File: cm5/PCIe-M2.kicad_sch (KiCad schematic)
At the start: 39 parts, among them J1 67910-5700, J4 0786463001, M1 M.2 Screw, M2 M.2 Solder Nut, M3 M.2 Solder Nut, M4 M.2 Solder Nut, M5 M.2 Solder Nut, U1 CAT24C128, U8 AP3441SHE-7B

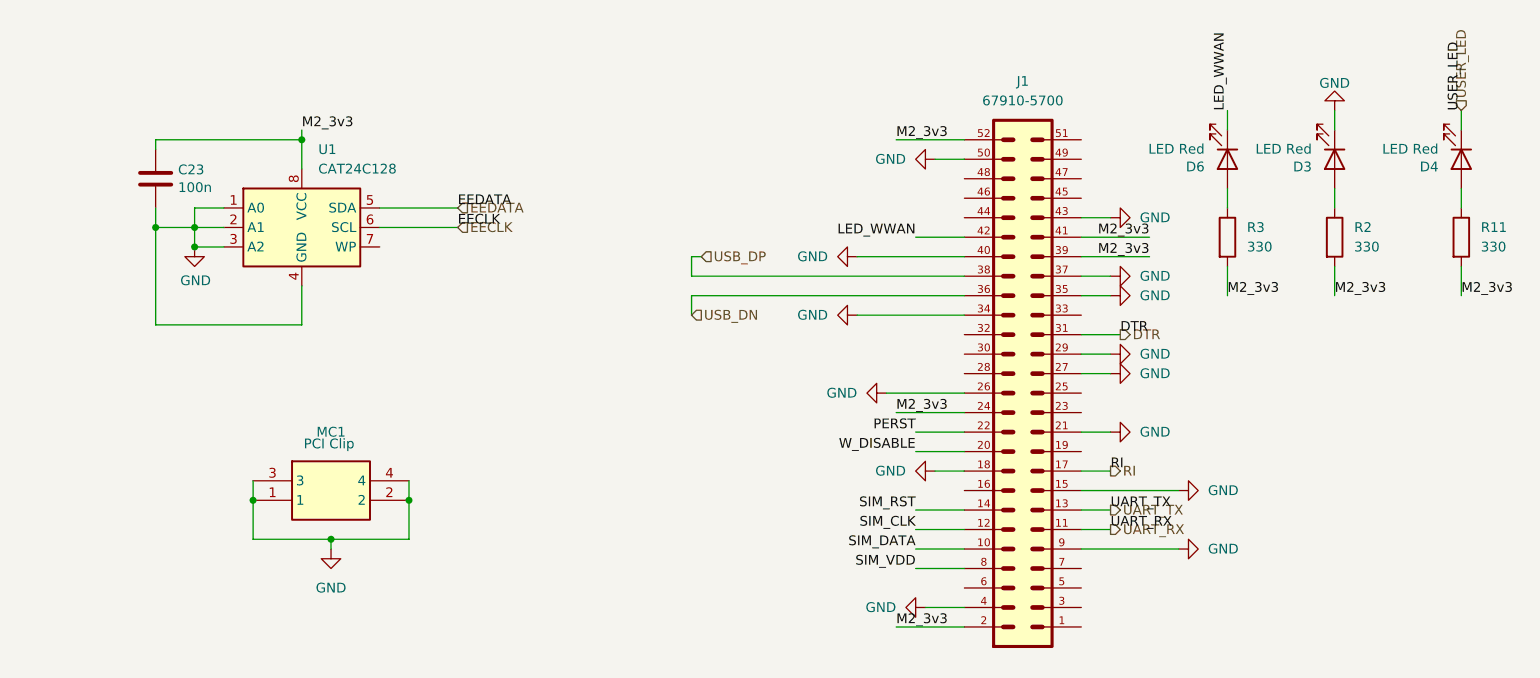
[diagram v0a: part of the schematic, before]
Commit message: Uh in this version, I have made the 5v trace fatter
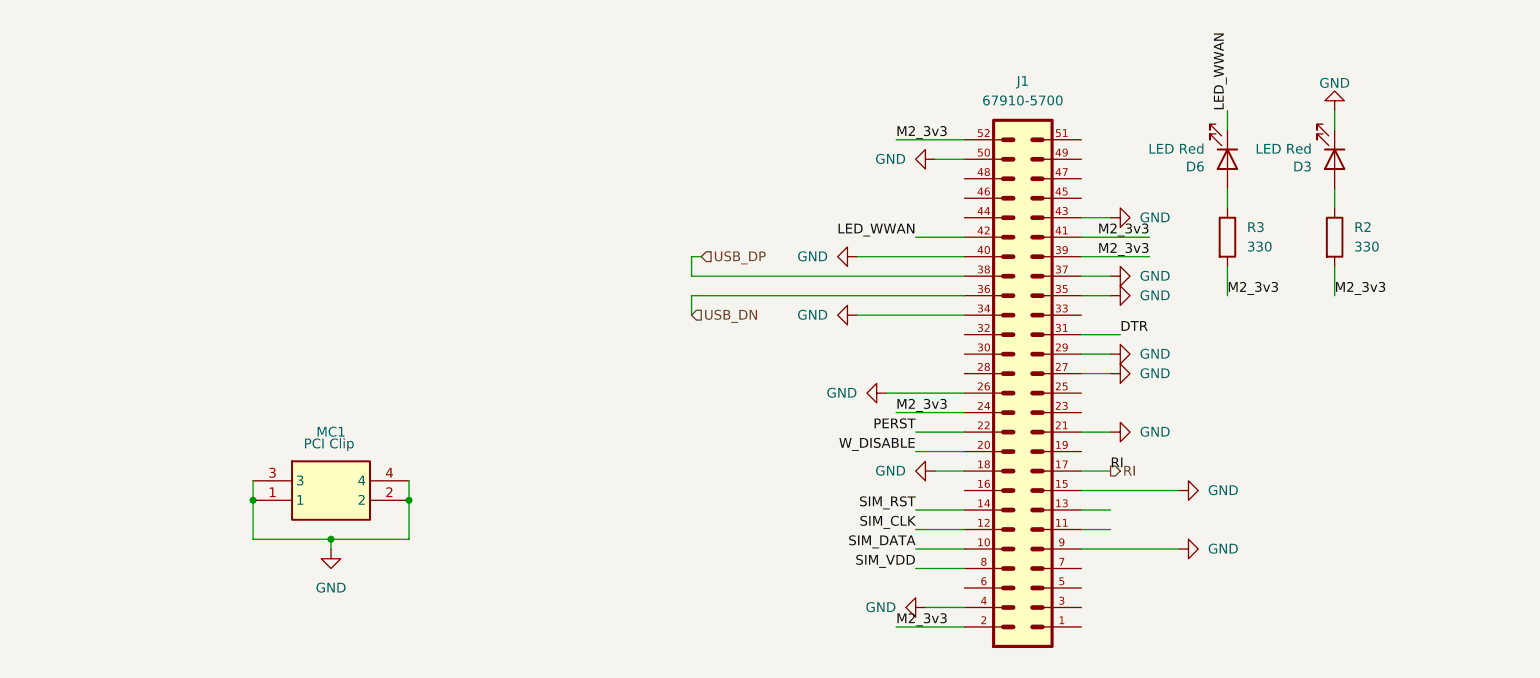
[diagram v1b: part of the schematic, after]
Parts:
- removed C23: 100n, Capacitor_SMD:C_0402_1005Metric, symbol Device:C
- removed D4: LED Red, LED_SMD:LED_0603_1608Metric, symbol Device:LED
- removed R11: 330, Resistor_SMD:R_0603_1608Metric, symbol Device:R
- removed U1: CAT24C128, Package_SO:SOIC-8_5.3x6.2mm_P1.27mm, symbol Memory_EEPROM:CAT24C128
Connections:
- net UART_RX: no longer names the net of J1.11
- net UART_TX: no longer names the net of J1.13

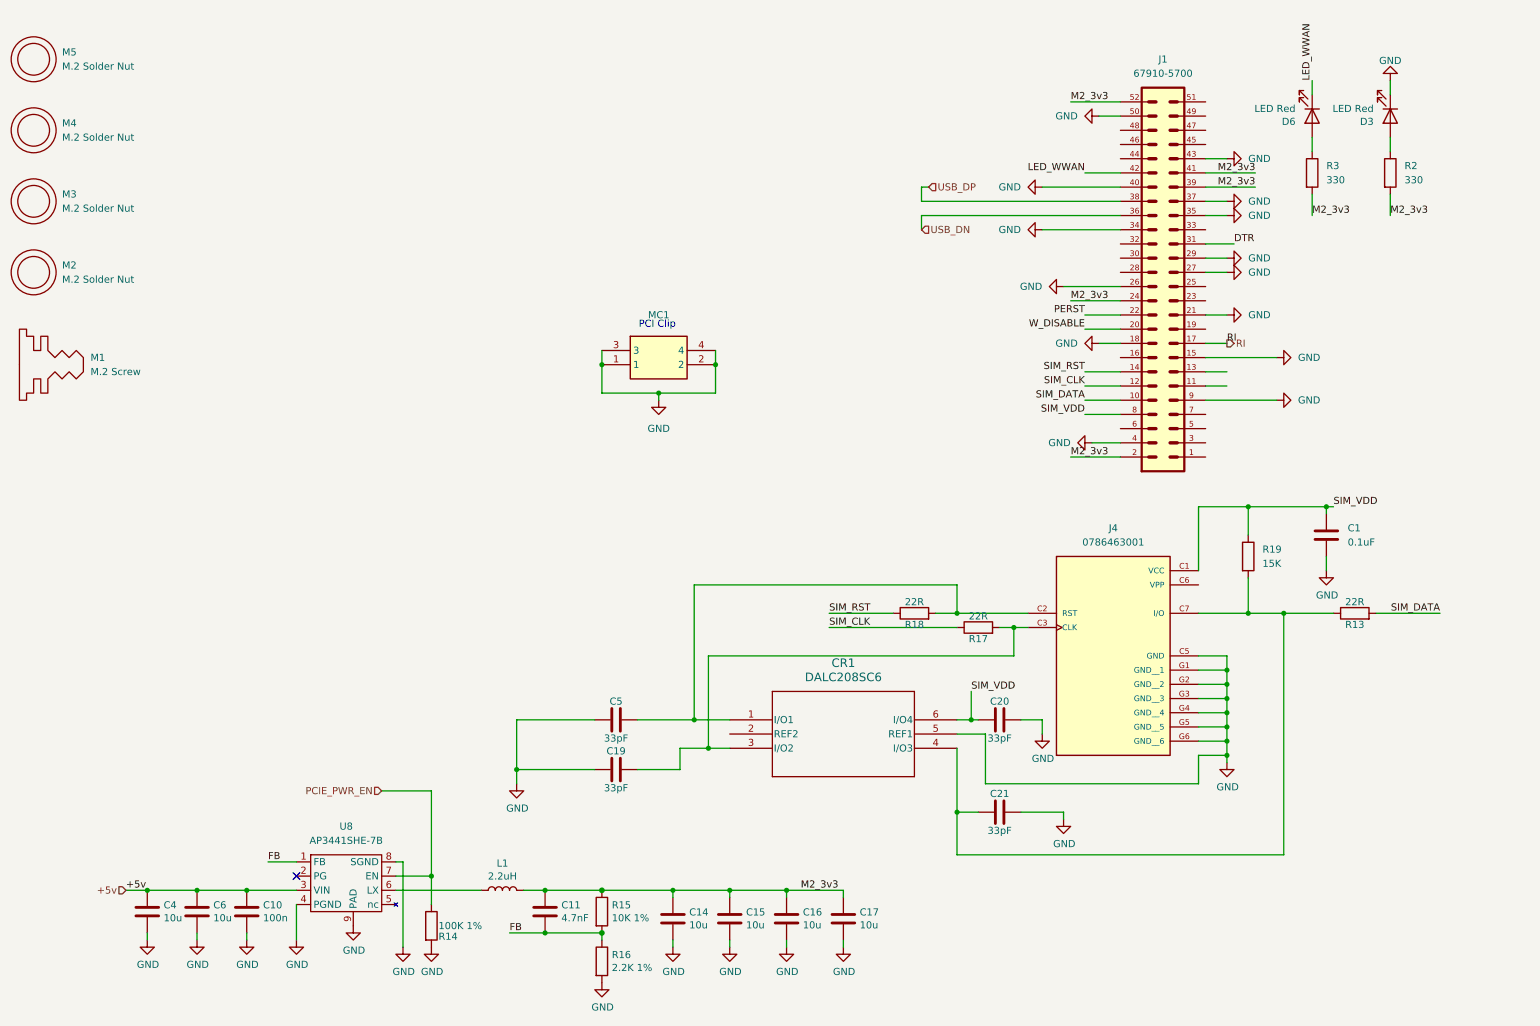
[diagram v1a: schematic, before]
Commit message: PCM1863 switchover (#5)
* Oops, basically brand new ADC design using a new chip

* Working PCB and working driver, sort of

* --amend
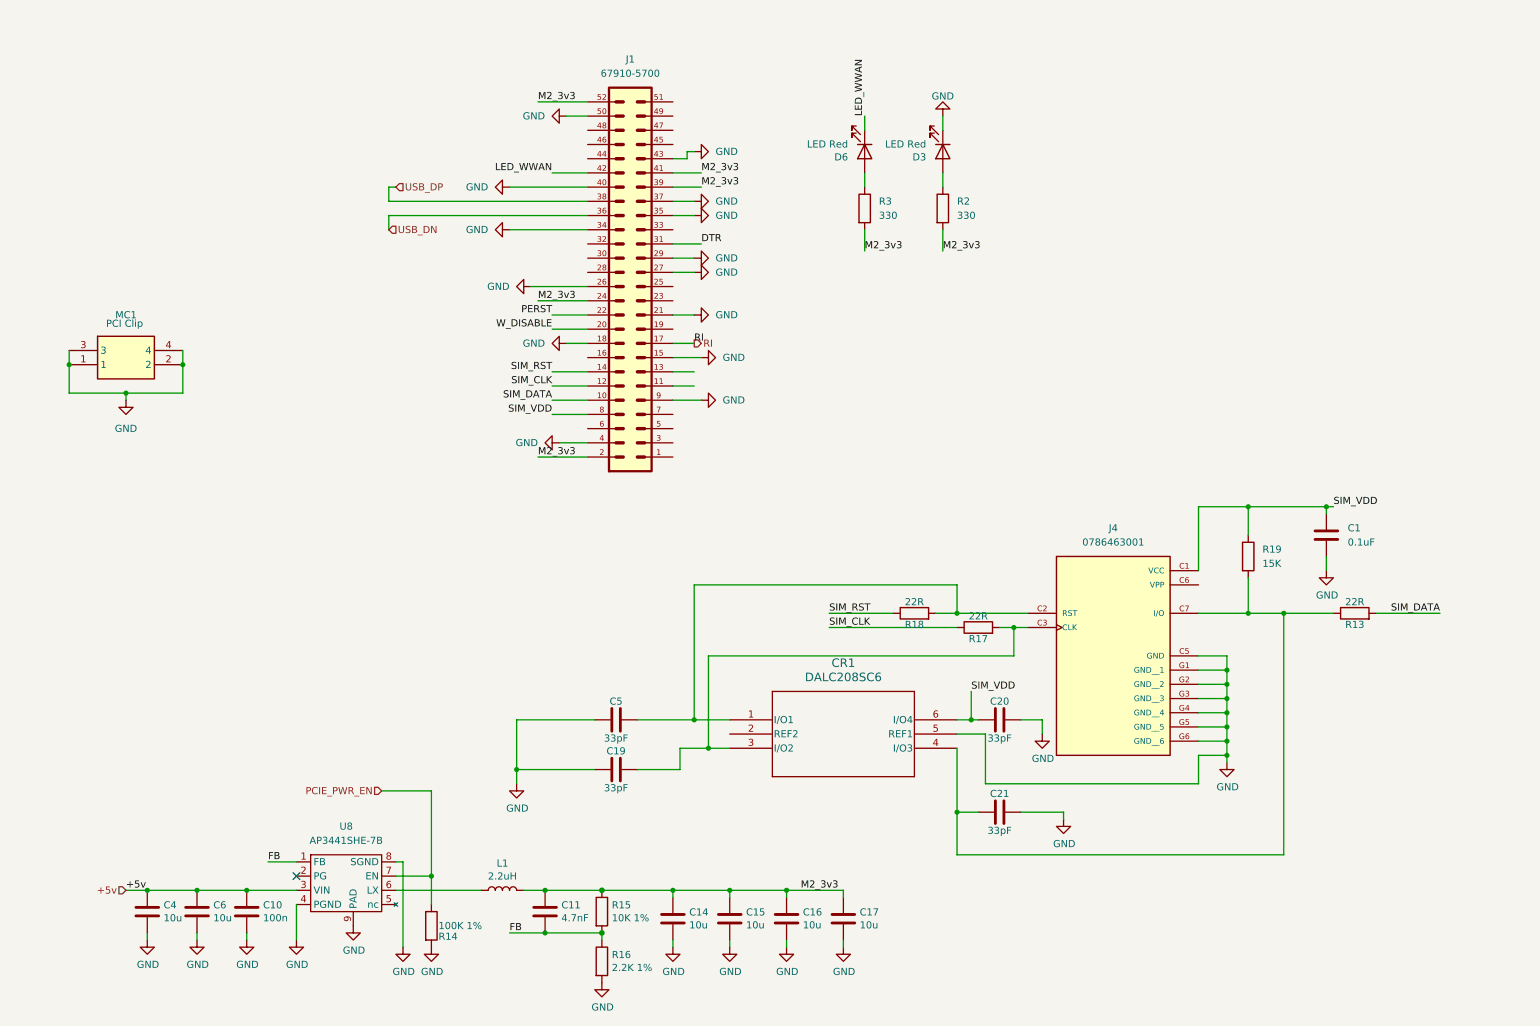
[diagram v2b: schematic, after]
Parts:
- removed M1: M.2 Screw, symbol CM5IO:M.2_Screw
- removed M2, M3, M4, M5: M.2 Solder Nut, symbol CM5IO:SolderNut
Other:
- moved on the sheet: D3, D6, J1, MC1, R2, R3
